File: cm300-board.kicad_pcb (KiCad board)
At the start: 2 copper layers, 48.3 x 25.4 mm, 11 parts, among them J1 Screw_Terminal_01x02, J2 Screw_Terminal_01x02, J3 Conn_01x04_Female

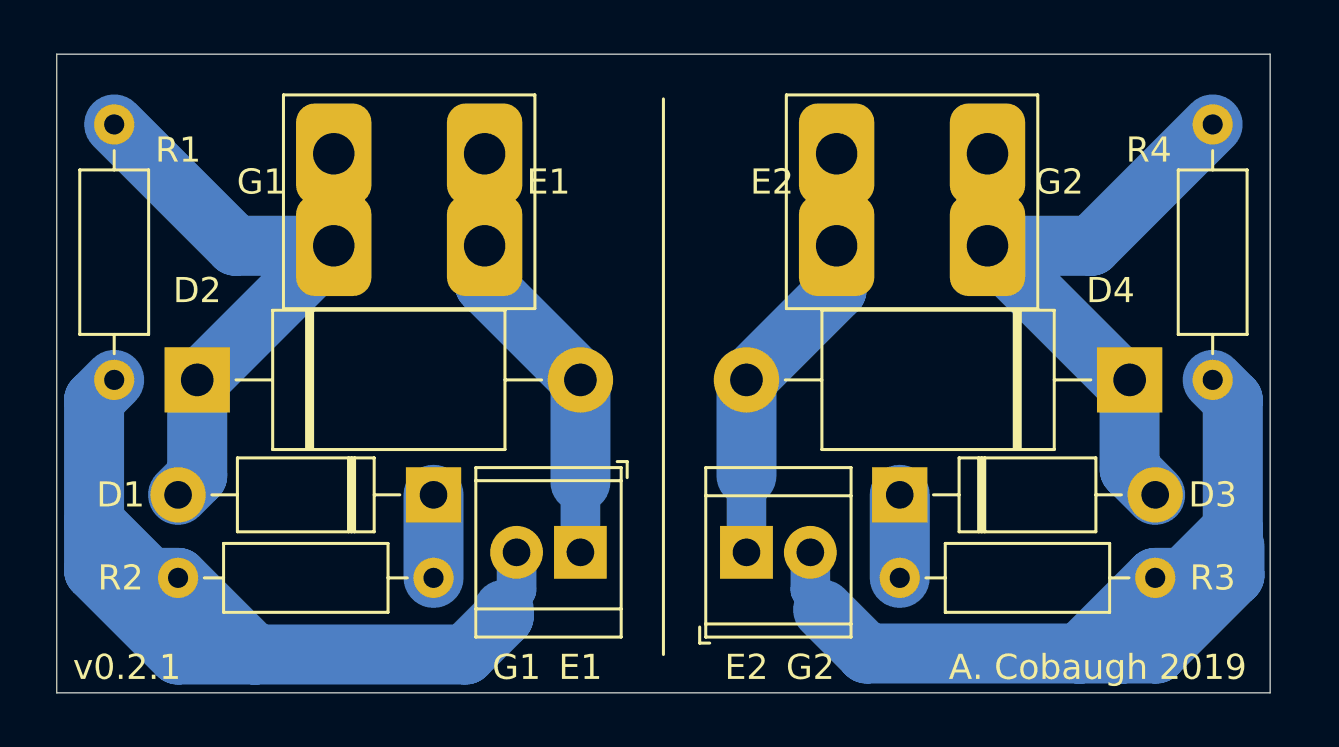
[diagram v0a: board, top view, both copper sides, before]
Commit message: switch to smd
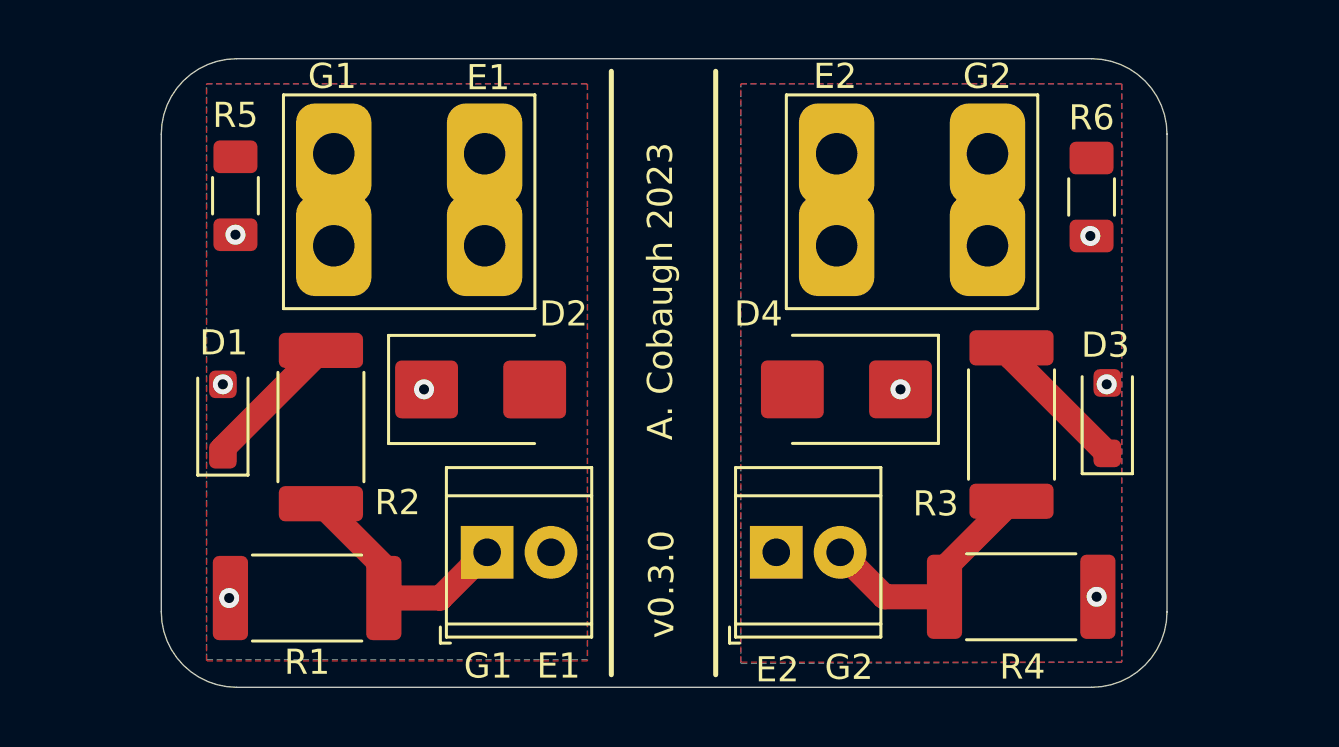
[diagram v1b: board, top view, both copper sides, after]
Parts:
- added R5: 10K, Resistor_SMD:R_1206_3216Metric_Pad1.30x1.75mm_HandSolder, F.Cu at (-1003.0, -1053.5)
- added R6: 10k, Resistor_SMD:R_1206_3216Metric_Pad1.30x1.75mm_HandSolder, F.Cu at (-969.0, -1053.5)
- D1, D3: footprint Diode_THT:D_DO-41_SOD81_P10.16mm_Horizontal -> Diode_SMD:D_SOD-123F
- D2, D4: footprint Diode_THT:D_DO-201AE_P15.24mm_Horizontal -> Diode_SMD:D_SMB
- R1, R2, R3, R4: footprint Resistor_THT:R_Axial_DIN0207_L6.3mm_D2.5mm_P10.16mm_Horizontal -> Resistor_SMD:R_2512_6332Metric_Pad1.40x3.35mm_HandSolder
- moved R1 20.3 mm to (-1000.2, -1037.5), turned to 0 degrees
- moved R4 20.3 mm to (-971.8, -1037.6), turned to 180 degrees
- moved D2 11.3 mm to (-993.3, -1045.8)
- moved D4 11.3 mm to (-978.8, -1045.8)
- moved D1 8.90 mm to (-1003.5, -1044.7), turned to 90 degrees
- moved D3 8.80 mm to (-968.4, -1044.7), turned to 90 degrees
- moved R3 7.55 mm to (-972.2, -1044.5), turned to -90 degrees
- moved R2 7.49 mm to (-999.6, -1044.3), turned to -90 degrees
- moved J1 3.71 mm to (-993.0, -1039.4), turned to 0 degrees
- moved J2 1.19 mm to (-981.5, -1039.4)
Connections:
- D2 pad 2: Net-(D2-Pad2) -> Net-(D2-A2)
- J1 pad 1: Net-(D2-Pad2) -> Net-(J1-Pin_1)
- J1 pad 2: Net-(J1-Pad2) -> Net-(D2-A2)
- J3 pad 2: Net-(D2-Pad2) -> Net-(D2-A2)
- R1 pad 2: Net-(J1-Pad2) -> Net-(J1-Pin_1)
- R2 pad 2: Net-(J1-Pad2) -> Net-(J1-Pin_1)
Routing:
- net Net-(J1-Pad2): track 37.5 -> 0.00 mm
- net Net-(J2-Pin_2): track 43.2 -> 9.79 mm
- net Net-(D3-A): track 24.1 -> 0.32 mm, vias 0 -> 4
- net Net-(D1-A): track 23.6 -> 0.35 mm, vias 0 -> 4
- net Net-(D2-Pad2): track 13.8 -> 0.00 mm
- net Net-(D4-A2): track 14.2 -> 1.01 mm
- net Net-(J1-Pin_1): track 0.00 -> 10.5 mm
- net Net-(D3-K): track 3.30 -> 5.77 mm
- net Net-(D1-K): track 3.30 -> 5.77 mm
- added copper zone on B.Cu, net Net-(D1-A)
- added copper zone on F.Cu, net Net-(D2-A2)
- added copper zone on B.Cu, net Net-(D3-A)
- added copper zone on F.Cu, net Net-(D4-A2)
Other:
- board size 48.3 x 25.4 mm -> 40 x 25 mm
- net class Default removed
- board text added: "A. Cobaugh 2023"
- board text added: "v0.3.0"
- board text removed: "A. Cobaugh 2019"
- board text removed: "v0.2.1"
